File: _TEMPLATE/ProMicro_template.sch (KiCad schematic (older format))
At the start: 6 parts

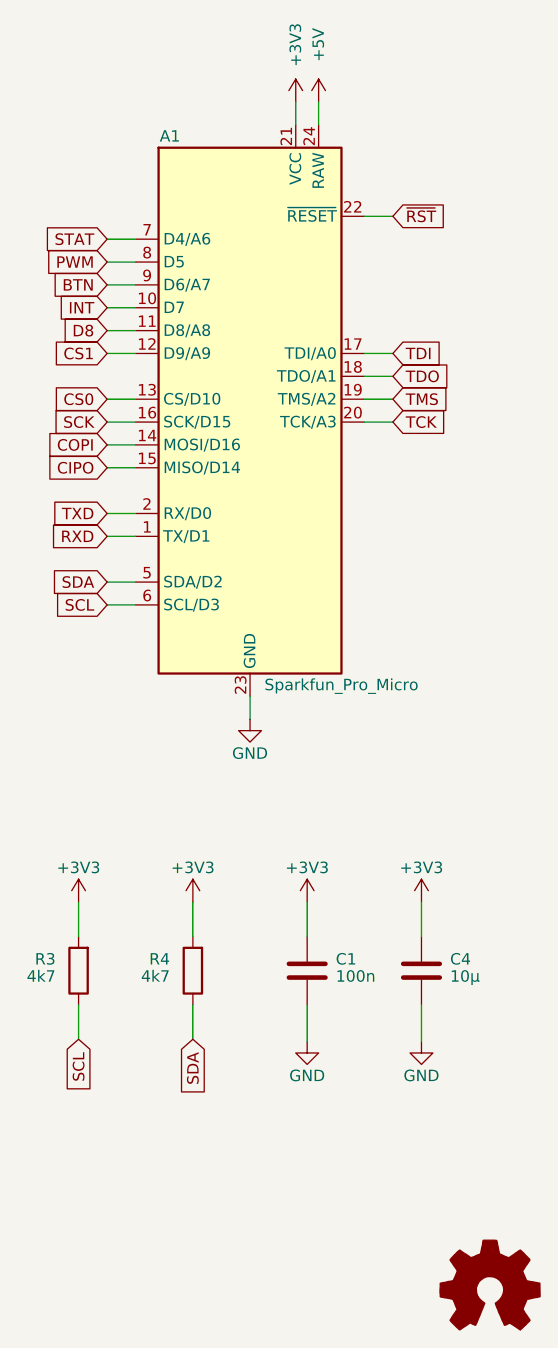
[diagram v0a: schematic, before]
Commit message: update PCBs to be stackable
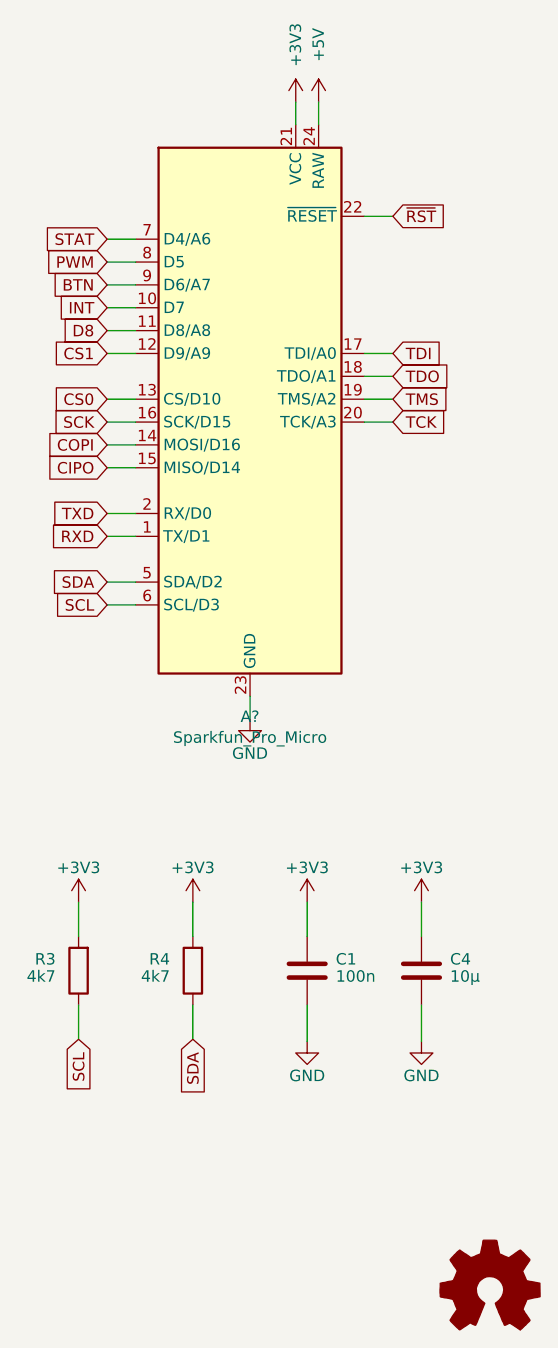
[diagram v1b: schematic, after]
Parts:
- removed A1: Sparkfun_Pro_Micro, Module:Sparkfun_Pro_Micro, symbol MCU_Module:Sparkfun_Pro_Micro
- added A?: Sparkfun_Pro_Micro, Module:Sparkfun_Pro_Micro, symbol ProMicro:Sparkfun_Pro_Micro
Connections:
- net +3V3: now also A?.21 (VCC)
- net +5V: now also A?.24 (RAW)
- net BTN: now also A?.9 (D6/A7)
- net CIPO: now also A?.15 (MISO/D14)
- net COPI: now also A?.14 (MOSI/D16)
- net CS0: now also A?.13 (CS/D10)
- net CS1: now also A?.12 (D9/A9)
- net D8: now also A?.11 (D8/A8)
- net GND: now also A?.23 (GND), A?.3 (GND), A?.4 (GND)
- net INT: now also A?.10 (D7)
- net PWM: now also A?.8 (D5)
- net RXD: now also A?.1 (TX/D1)
- net SCK: now also A?.16 (SCK/D15)
- net SCL: now also A?.6 (SCL/D3)
- net SDA: now also A?.5 (SDA/D2)
- net STAT: now also A?.7 (D4/A6)
- net TCK: now also A?.20 (TCK/A3)
- net TDI: now also A?.17 (TDI/A0)
- net TDO: now also A?.18 (TDO/A1)
- net TMS: now also A?.19 (TMS/A2)
- net TXD: now also A?.2 (RX/D0)
- net ~RST: now also A?.22 (~RESET)
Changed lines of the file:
@@
 Text GLabel 9125 3800 0    50   Input ~ 0
 SDA
-$Comp
-L MCU_Module:Sparkfun_Pro_Micro A1
-U 1 1 5F84D072
-P 9750 3000
-F 0 "A1" H 9400 4150 50  0000 C CNN
-F 1 "Sparkfun_Pro_Micro" H 10150 1750 50  0000 C CNN
-F 2 "Module:Sparkfun_Pro_Micro" H 9850 1650 50  0001 L CNN
-F 3 "https://cdn.sparkfun.com/datasheets/Dev/Arduino/Boards/Pro_Micro_v13b.pdf" H 9750 2200 50  0001 C CNN
-	1    9750 3000
-	1    0    0    -1
-$EndComp
 Wire Wire Line
 	10050 1700 10050 1800
@@
 Wire Wire Line
 	10375 2800 10250 2800
+$Comp
+L ProMicro:Sparkfun_Pro_Micro A?
+U 1 1 5FB97DAC
+P 9750 3000
+F 0 "A?" H 9750 1611 50  0000 C CNN
+F 1 "Sparkfun_Pro_Micro" H 9750 1520 50  0000 C CNN
+F 2 "Module:Sparkfun_Pro_Micro" H 9850 1650 50  0001 L CNN
+F 3 "" H 9750 2200 50  0001 C CNN
+	1    9750 3000
+	1    0    0    -1
+$EndComp
 $EndSCHEMATC
